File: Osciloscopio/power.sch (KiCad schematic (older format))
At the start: 14 parts, among them U1 MAX232, U2 78L05, U3 79L05

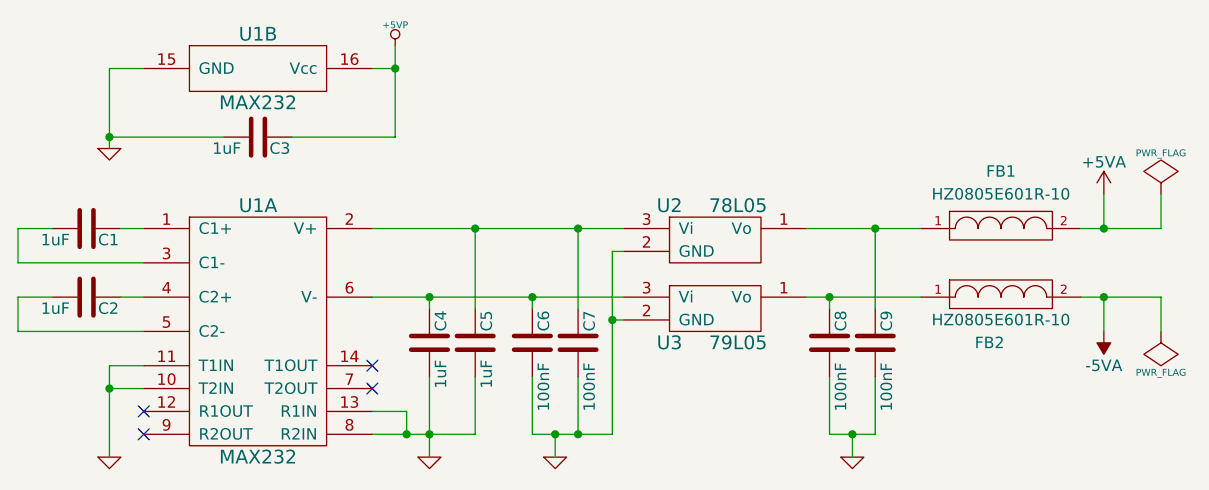
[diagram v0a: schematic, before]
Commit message: Se definen los footprints y numeros de parte de todos los componentes Se elimina el Boton de Gain dado que un solo boton es insuficiente para controlar el osciloscopio y no se disponen de señales digitales suficientes para controlar varios botones. Se decide por ende colocar el display cerca de los botones de la EDU-CIAA de modo que se pueda colocar en el display la función de los botones.
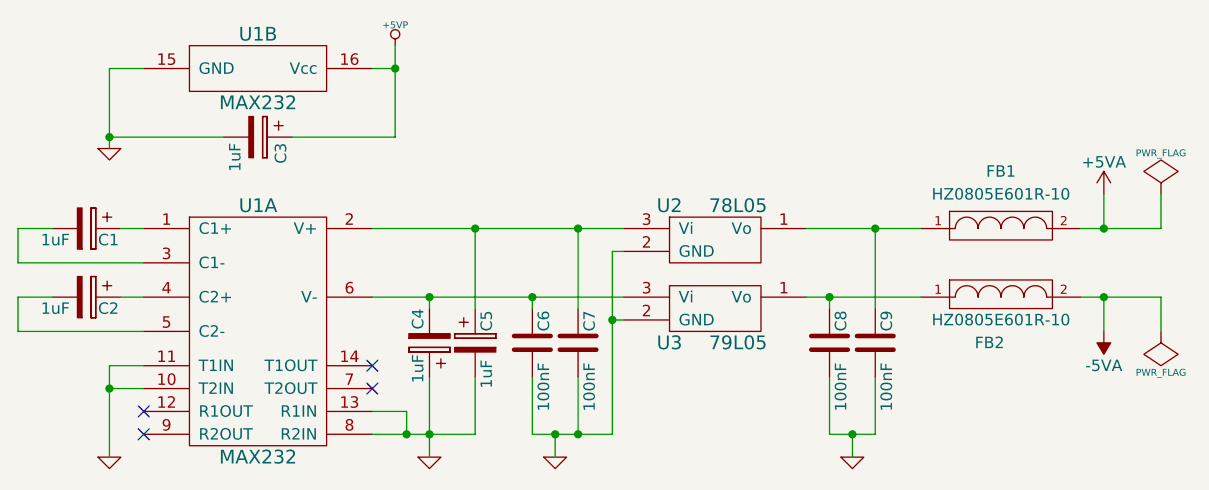
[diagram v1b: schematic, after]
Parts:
- removed C1, C2, C3, C4, C5: 1uF, symbol C
- added C1, C2, C3, C4, C5: 1uF, Capacitors_ThroughHole:C_Radial_D5_L11_P2, symbol CP
- C6, C7, C8, C9: footprint (none) -> Capacitors_SMD:C_0805_HandSoldering; Digikey# (none) -> 1276-6468-1-ND; Manf (none) -> Samsung Electro-Mechanics America, Inc.; Manf# (none) -> CL21B104KBFNNNG
- FB1, FB2: footprint (none) -> Resistors_SMD:R_0805_HandSoldering; Digikey# (none) -> 240-2399-1-ND; Manf (none) -> Laird-Signal Integrity Products; Manf# (none) -> HZ0805E601R-10
- U1: footprint (none) -> Housings_DIP:DIP-16_W7.62mm_LongPads
- U2: footprint (none) -> TO_SOT_Packages_THT:TO-92_Inline_Wide; Digikey# (none) -> 296-1365-1-ND; Manf (none) -> Texas Instruments; Manf# (none) -> UA78L05ACLPR
- U3: footprint (none) -> TO_SOT_Packages_THT:TO-92_Inline_Wide; Digikey# (none) -> 296-31456-1-ND; Manf (none) -> Texas Instruments; Manf# (none) -> MC79L05ACLPR
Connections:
- net +5VP: now also C3.1
- net GND: now also C3.2, C4.1, C5.2
- net at U1.1 (C1+): now also C1.1
- net at C7.1, U1.2 (V+), U2.3 (Vi): now also C5.1
- net at U1.3 (C1-): now also C1.2
- net at U1.4 (C2+): now also C2.1
- net at U1.5 (C2-): now also C2.2
- net at C6.1, U1.6 (V-), U3.3 (Vi): now also C4.2

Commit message: Ultimas correciones de la revisión
_ Se copian localmente footprints y se los linkead
_ Se copian localmente los modelos 3D y se los linkea
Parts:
- C1, C2, C3, C4, C5: footprint Capacitors_ThroughHole:C_Radial_D5_L11_P2 -> osc:C_Radial_D5_L11_P2
- C6, C7, C8, C9: footprint Capacitors_SMD:C_0805_HandSoldering -> osc:C_0805_HandSoldering
- FB1, FB2: footprint Resistors_SMD:R_0805_HandSoldering -> osc:R_0805_HandSoldering
- U1: footprint Housings_DIP:DIP-16_W7.62mm_LongPads -> osc:DIP-16_W7.62mm_LongPads
- U2, U3: footprint TO_SOT_Packages_THT:TO-92_Inline_Wide -> osc:TO-92_Inline_Wide
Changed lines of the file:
@@
 F 0 "U1" H 3950 4400 60  0000 C CNN
 F 1 "MAX232" H 3950 3300 60  0000 C CNN
-F 2 "Housings_DIP:DIP-16_W7.62mm_LongPads" H 3950 3900 60  0001 C CNN
+F 2 "osc:DIP-16_W7.62mm_LongPads" H 3950 3900 60  0001 C CNN
 F 3 "" H 3950 3900 60  0000 C CNN
 F 4 "296-1402-5-ND" H 3950 3850 60  0001 C CNN "Digikey#"
@@
 F 0 "FB2" H 7150 3500 50  0000 C CNN
 F 1 "HZ0805E601R-10" H 7200 3600 50  0000 C CNN
-F 2 "Resistors_SMD:R_0805_HandSoldering" H 7200 3700 50  0001 C CNN
+F 2 "osc:R_0805_HandSoldering" H 7200 3700 50  0001 C CNN
 F 3 "" H 7200 3700 50  0000 C CNN
 F 4 "240-2399-1-ND" H 7200 3700 60  0001 C CNN "Digikey#"
@@
 F 0 "FB1" H 7200 3650 50  0000 C CNN
 F 1 "HZ0805E601R-10" H 7200 3550 50  0000 C CNN
-F 2 "Resistors_SMD:R_0805_HandSoldering" H 7200 3400 50  0001 C CNN
+F 2 "osc:R_0805_HandSoldering" H 7200 3400 50  0001 C CNN
 F 3 "" H 7200 3400 50  0000 C CNN
 F 4 "240-2399-1-ND" H 7200 3400 60  0001 C CNN "Digikey#"
@@
 F 0 "U1" H 3950 2850 60  0000 C CNN
 F 1 "MAX232" H 3950 2550 60  0000 C CNN
-F 2 "Housings_DIP:DIP-16_W7.62mm_LongPads" H 3950 2750 60  0001 C CNN
+F 2 "osc:DIP-16_W7.62mm_LongPads" H 3950 2750 60  0001 C CNN
 F 3 "" H 3950 2750 60  0000 C CNN
 F 4 "296-1402-5-ND" H 3950 2700 60  0001 C CNN "Digikey#"
@@
 F 0 "U3" H 5750 3600 60  0000 C CNN
 F 1 "79L05" H 6050 3600 60  0000 C CNN
-F 2 "TO_SOT_Packages_THT:TO-92_Inline_Wide" H 5950 3750 60  0001 C CNN
+F 2 "osc:TO-92_Inline_Wide" H 5950 3750 60  0001 C CNN
 F 3 "" H 5950 3750 60  0000 C CNN
 F 4 "296-31456-1-ND" H 5950 3750 60  0001 C CNN "Digikey#"
@@
 F 0 "U2" H 5750 3600 60  0000 C CNN
 F 1 "78L05" H 6050 3600 60  0000 C CNN
-F 2 "TO_SOT_Packages_THT:TO-92_Inline_Wide" H 5950 3450 60  0001 C CNN
+F 2 "osc:TO-92_Inline_Wide" H 5950 3450 60  0001 C CNN
 F 3 "" H 5950 3450 60  0000 C CNN
 F 4 "296-1365-1-ND" H 5950 3450 60  0001 C CNN "Digikey#"
@@
 F 0 "C6" V 5200 3950 50  0000 L CNN
 F 1 "100nF" V 5200 3600 50  0000 L CNN
-F 2 "Capacitors_SMD:C_0805_HandSoldering" H 5188 3750 50  0001 C CNN
+F 2 "osc:C_0805_HandSoldering" H 5188 3750 50  0001 C CNN
 F 3 "" H 5150 3900 50  0000 C CNN
 F 4 "1276-6468-1-ND" H 5150 3900 60  0001 C CNN "Digikey#"
@@
 F 0 "C3" H 3975 3100 50  0000 L CNN
 F 1 "1uF" H 3975 2900 50  0000 L CNN
-F 2 "Capacitors_ThroughHole:C_Radial_D5_L11_P2" H 3988 2850 50  0001 C CNN
+F 2 "osc:C_Radial_D5_L11_P2" H 3988 2850 50  0001 C CNN
 F 3 "" H 3950 3000 50  0000 C CNN
 F 4 "732-8851-1-ND" H 3950 3000 60  0001 C CNN "Digikey#"
@@
 F 0 "C1" V 3250 3450 50  0000 L CNN
 F 1 "1uF" V 3250 3200 50  0000 L CNN
-F 2 "Capacitors_ThroughHole:C_Radial_D5_L11_P2" H 3238 3250 50  0001 C CNN
+F 2 "osc:C_Radial_D5_L11_P2" H 3238 3250 50  0001 C CNN
 F 3 "" H 3200 3400 50  0000 C CNN
 F 4 "732-8851-1-ND" H 3200 3400 60  0001 C CNN "Digikey#"
@@
 F 0 "C2" V 3250 3750 50  0000 L CNN
 F 1 "1uF" V 3250 3500 50  0000 L CNN
-F 2 "Capacitors_ThroughHole:C_Radial_D5_L11_P2" H 3238 3550 50  0001 C CNN
+F 2 "osc:C_Radial_D5_L11_P2" H 3238 3550 50  0001 C CNN
 F 3 "" H 3200 3700 50  0000 C CNN
 F 4 "732-8851-1-ND" H 3200 3700 60  0001 C CNN "Digikey#"
@@
 F 0 "C4" V 4750 3750 50  0000 L CNN
 F 1 "1uF" V 4750 3950 50  0000 L CNN
-F 2 "Capacitors_ThroughHole:C_Radial_D5_L11_P2" H 4738 3750 50  0001 C CNN
+F 2 "osc:C_Radial_D5_L11_P2" H 4738 3750 50  0001 C CNN
 F 3 "" H 4700 3900 50  0000 C CNN
 F 4 "732-8851-1-ND" H 4700 3900 60  0001 C CNN "Digikey#"
@@
 F 0 "C5" V 4950 3950 50  0000 L CNN
 F 1 "1uF" V 4950 3700 50  0000 L CNN
-F 2 "Capacitors_ThroughHole:C_Radial_D5_L11_P2" H 4938 3750 50  0001 C CNN
+F 2 "osc:C_Radial_D5_L11_P2" H 4938 3750 50  0001 C CNN
 F 3 "" H 4900 3900 50  0000 C CNN
 F 4 "732-8851-1-ND" H 4900 3900 60  0001 C CNN "Digikey#"
@@
 F 0 "C7" V 5400 3950 50  0000 L CNN
 F 1 "100nF" V 5400 3600 50  0000 L CNN
-F 2 "Capacitors_SMD:C_0805_HandSoldering" H 5388 3750 50  0001 C CNN
+F 2 "osc:C_0805_HandSoldering" H 5388 3750 50  0001 C CNN
 F 3 "" H 5350 3900 50  0000 C CNN
 F 4 "1276-6468-1-ND" H 5350 3900 60  0001 C CNN "Digikey#"
@@
 F 0 "C8" V 6500 3950 50  0000 L CNN
 F 1 "100nF" V 6500 3600 50  0000 L CNN
-F 2 "Capacitors_SMD:C_0805_HandSoldering" H 6488 3750 50  0001 C CNN
+F 2 "osc:C_0805_HandSoldering" H 6488 3750 50  0001 C CNN
 F 3 "" H 6450 3900 50  0000 C CNN
 F 4 "1276-6468-1-ND" H 6450 3900 60  0001 C CNN "Digikey#"
@@
 F 0 "C9" V 6700 3950 50  0000 L CNN
 F 1 "100nF" V 6700 3600 50  0000 L CNN
-F 2 "Capacitors_SMD:C_0805_HandSoldering" H 6688 3750 50  0001 C CNN
+F 2 "osc:C_0805_HandSoldering" H 6688 3750 50  0001 C CNN
 F 3 "" H 6650 3900 50  0000 C CNN
 F 4 "1276-6468-1-ND" H 6650 3900 60  0001 C CNN "Digikey#"
